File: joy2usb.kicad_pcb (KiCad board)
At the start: 2 copper layers, 55 x 90 mm, 18 parts, among them J1 DB9_Male, J2 Conn_02x04_Odd_Even, SW1 RST, SW2 SW_SPDT, U1 Arduino_Pro_Micro, U2 4066

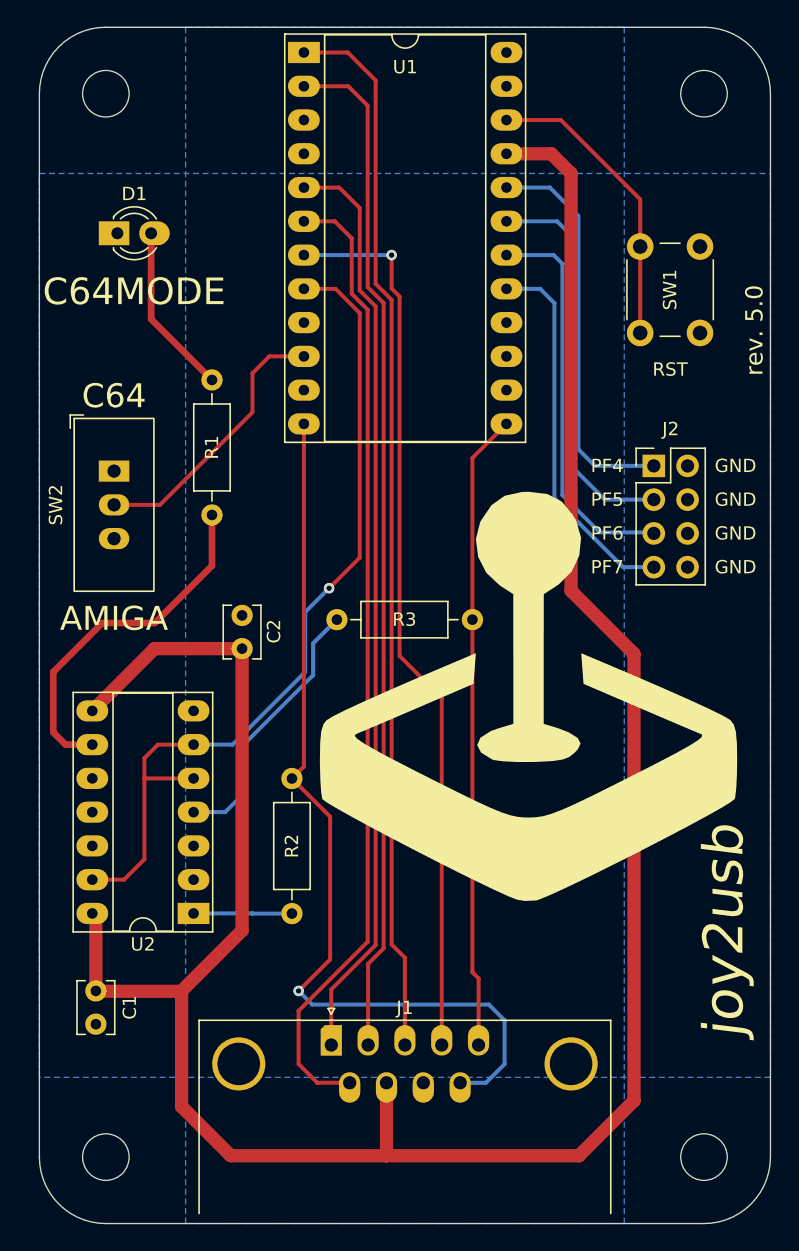
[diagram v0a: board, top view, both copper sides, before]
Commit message: PCB Rev. 6.2
removal of ic 4066
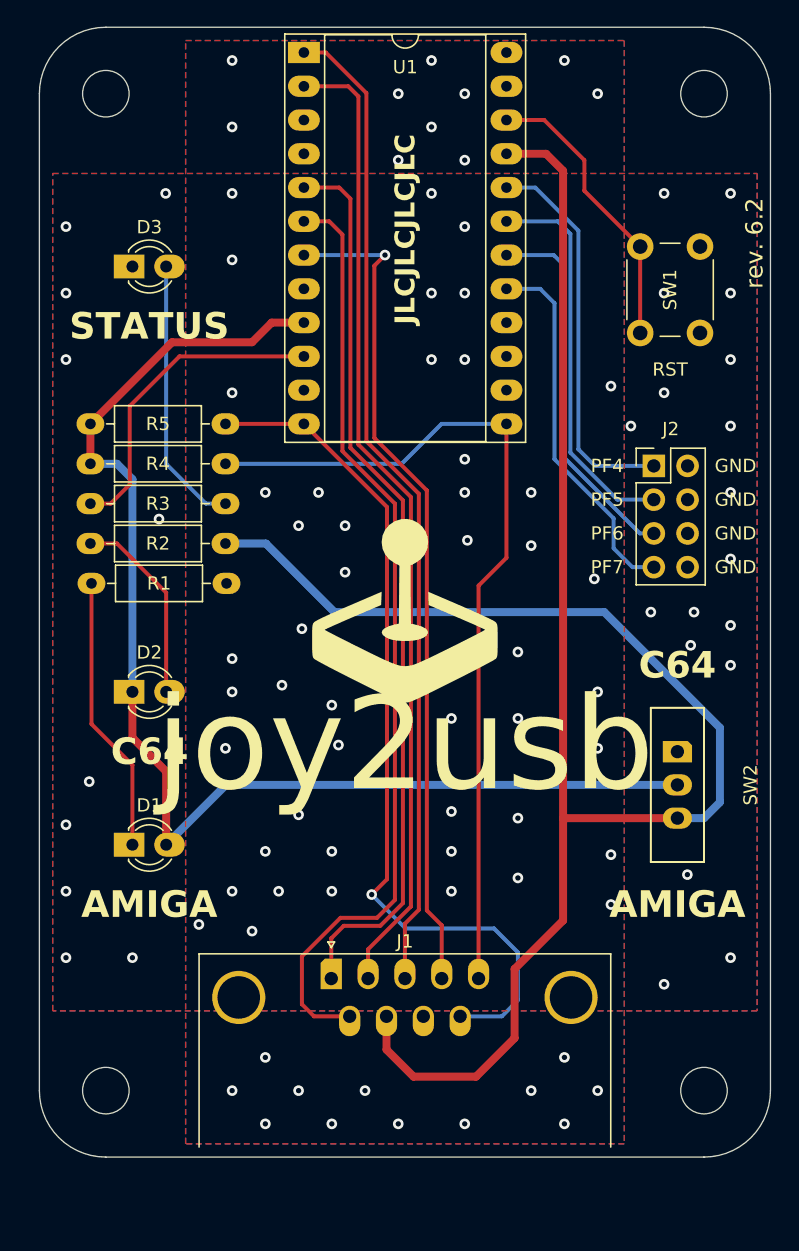
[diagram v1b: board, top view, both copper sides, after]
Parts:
- removed C1, C2: 100nF, Capacitor_THT:C_Disc_D3.8mm_W2.6mm_P2.50mm
- removed the G*** at (149.8, 105.5)
- removed REF**: OSHW-Logo_28.5x30mm_SilkScreen, Symbol:OSHW-Logo_28.5x30mm_SilkScreen
- removed U2: 4066, Package_DIP:DIP-14_W7.62mm_Socket_LongPads
- added D2: C64, misc:LED_D3.0mm_Oval, F.Cu at (120.0, 105.0)
- added D3: STATUS, misc:LED_D3.0mm_Oval, F.Cu at (120.0, 73.0)
- added G***: LOGO, misc:Joystick_LOGO_14x14mm, F.Cu at (140.5, 99.0)
- added R4: R10KΩ, misc:R_Axial_DIN0207_L6.3mm_D2.5mm_P10.16mm_Horizontal_Oval, F.Cu at (127.0, 87.8)
- added R5: RxΩ, misc:R_Axial_DIN0207_L6.3mm_D2.5mm_P10.16mm_Horizontal_Oval, F.Cu at (127.0, 84.8)
- D1: value C64MODE -> AMIGA; footprint Misc:LED_D3.0mm_Oval -> misc:LED_D3.0mm_Oval
- R1: value R220Ω -> RxΩ; footprint Resistor_THT:R_Axial_DIN0207_L6.3mm_D2.5mm_P10.16mm_Horizontal -> misc:R_Axial_DIN0207_L6.3mm_D2.5mm_P10.16mm_Horizontal_Oval
- R2: value R10KΩ -> RxΩ; footprint Resistor_THT:R_Axial_DIN0207_L6.3mm_D2.5mm_P10.16mm_Horizontal -> misc:R_Axial_DIN0207_L6.3mm_D2.5mm_P10.16mm_Horizontal_Oval
- R3: footprint Resistor_THT:R_Axial_DIN0207_L6.3mm_D2.5mm_P10.16mm_Horizontal -> misc:R_Axial_DIN0207_L6.3mm_D2.5mm_P10.16mm_Horizontal_Oval
- SW2: value SW_SPDT -> C64MODESW; footprint Misc:MFP_1220_KNITTER_SWITCH_SPDT_Oval -> misc:E-Switch-EG1218-Manufacturer_Recommended_Oval
- moved SW2 51.6 mm to (161.0, 109.5), turned to -90 degrees
- moved D1 46.0 mm to (120.0, 116.5)
- moved R3 20.5 mm to (127.0, 90.8)
- moved R2 18.4 mm to (127.0, 93.8), turned to 180 degrees
- moved R1 5.26 mm to (127.1, 96.8), turned to 180 degrees
- moved H1 5.00 mm to (118.0, 135.0)
- moved H4 5.00 mm to (163.0, 135.0)
- moved J1 5.00 mm to (135.0, 126.6)
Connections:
- D1 pad 1: GND -> Net-(D1-K)
- D1 pad 2: Net-(D1-Pad2) -> /F2F3MODE
- R1 pad 1: Net-(R1-Pad1) -> GND
- R1 pad 2: Net-(D1-Pad2) -> Net-(D1-K)
- R2 pad 1: /F2BTN -> VCC
- R3 pad 1: /F3BTN -> Net-(D3-A)
- R3 pad 2: Net-(U2-Pad4) -> Net-(U1-Digital7/PE6)
- SW2 pad 2: Net-(SW2-Pad2) -> /F2F3MODE
- SW2 pad 3: unconnected-(SW2-Pad3) -> VCC
- U1 pad 10: Net-(SW2-Pad2) -> Net-(U1-Digital7/PE6)
- U1 pad 8: /F2F3MODE -> unconnected-(U1-Digital5/PC6-Pad8)
- U1 pad 9: unconnected-(U1-Pad9) -> /F2F3MODE
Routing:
- net VCC: track 181.9 -> 146.6 mm
- net /F2F3MODE: track 64.3 -> 94.7 mm, vias 1 -> 0
- net Net-(R1-Pad1): track 26.9 -> 0.00 mm
- net Net-(U1-Digital7/PE6): track 0.00 -> 24.1 mm
- net Net-(D1-K): track 0.00 -> 20.9 mm
- net Net-(D3-A): track 0.00 -> 20.7 mm
- net Net-(SW2-Pad2): track 20.6 -> 0.00 mm
- net Net-(U2-Pad4): track 20.3 -> 0.00 mm
- net /F3BTN: track 47.9 -> 65.0 mm
- net Net-(D1-Pad2): track 12.9 -> 0.00 mm
- net Net-(D2-A): track 6.98 -> 14.7 mm
- net /LBTN: track 79.8 -> 74.7 mm
- net /RBTN: track 67.6 -> 63.0 mm
- net /DBTN: track 77.1 -> 73.8 mm
- net /F2BTN: track 68.8 -> 66.1 mm
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- added copper zone on F.Cu, net GND
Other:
- board size 55 x 90 mm -> 55 x 85 mm
- board text added: "JLCJLCJLCJLC"

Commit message: PCB Rev. 6.3
WayWayWay text on silkscreen for PCBWay is added
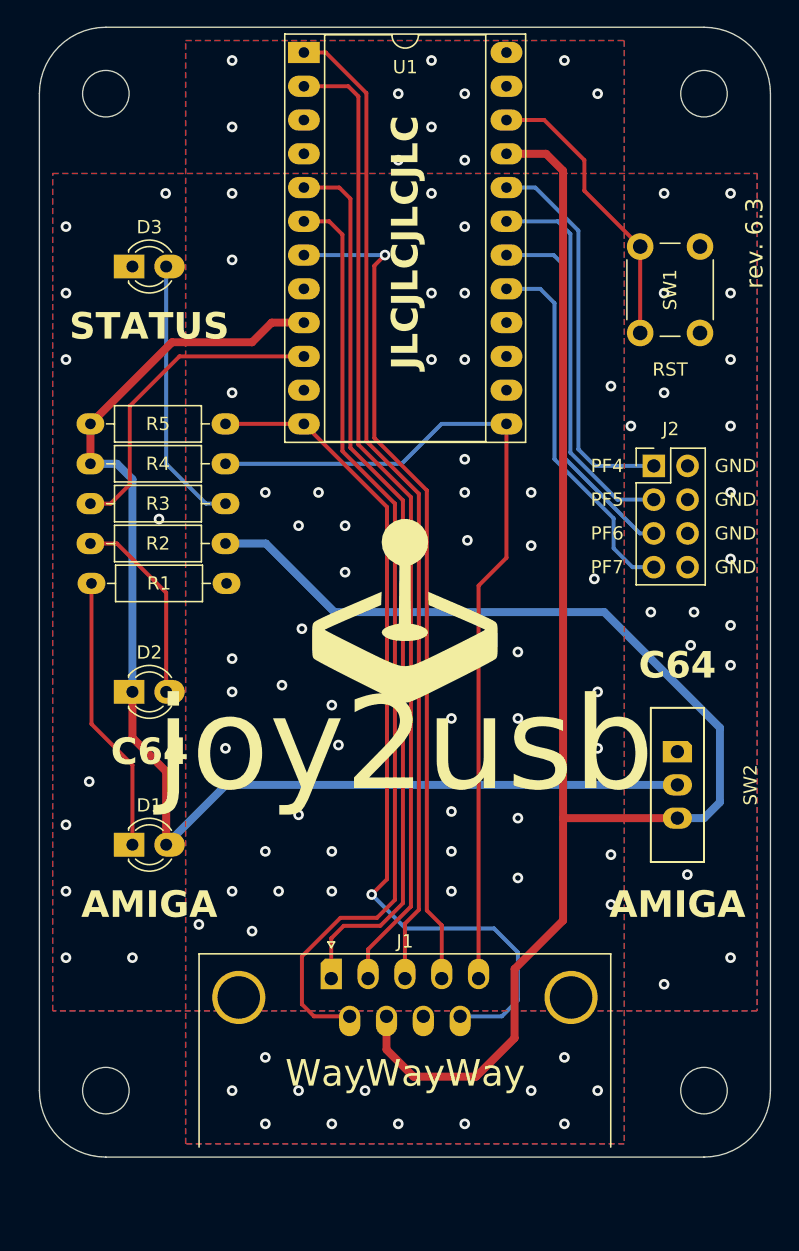
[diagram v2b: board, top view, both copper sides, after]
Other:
- board text added: "WayWayWay"
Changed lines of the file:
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@@
   (title_block
     (title "joy2usb")
-    (rev "6.2")
+    (rev "6.3")
     (company "mistepien@wp.pl")
   )
@@
     (effects (font (size 1.3 1.3) (thickness 0.3)))
   )
+  (gr_text "WayWayWay" (at 140.52 133.7) (layer "F.SilkS")
+    (effects (font (size 2 2) (thickness 0.3)))
+  )
   (gr_text "${TITLE}" (at 140.5 109) (layer "F.SilkS")
     (effects (font (face "C64") (size 7 7) (thickness 0.5)))
@@
     )
   )
-  (gr_text "JLCJLCJLCJLC" (at 140.52 70.2 90) (layer "F.SilkS")
-    (effects (font (size 1.5 1.5) (thickness 0.3) bold))
+  (gr_text "JLCJLCJLCJLC" (at 140.52 71.2 90) (layer "F.SilkS")
+    (effects (font (size 2 2) (thickness 0.3) bold))
   )
   (dimension (type aligned) (layer "Dwgs.User")
@@
   (segment (start 141.55 121.395584) (end 140.5 122.445584) (width 0.3) (layer "F.Cu") (net 3))
   (segment (start 142.15 121.444112) (end 143.27 122.564112) (width 0.3) (layer "F.Cu") (net 4))
+  (segment (start 142.15 89.84736) (end 142.15 121.444112) (width 0.3) (layer "F.Cu") (net 4))
+  (segment (start 143.27 122.564112) (end 143.27 126.569669) (width 0.3) (layer "F.Cu") (net 4))
+  (segment (start 138.2 72.94) (end 138.2 85.89736) (width 0.3) (layer "F.Cu") (net 4))
   (segment (start 139 72.14) (end 138.2 72.94) (width 0.3) (layer "F.Cu") (net 4))
   (segment (start 138.2 85.89736) (end 142.15 89.84736) (width 0.3) (layer "F.Cu") (net 4))
-  (segment (start 142.15 89.84736) (end 142.15 121.444112) (width 0.3) (layer "F.Cu") (net 4))
-  (segment (start 138.2 72.94) (end 138.2 85.89736) (width 0.3) (layer "F.Cu") (net 4))
-  (segment (start 143.27 122.564112) (end 143.27 126.569669) (width 0.3) (layer "F.Cu") (net 4))
   (via (at 139 72.14) (size 0.8) (drill 0.4) (layers "F.Cu" "B.Cu") (net 4))
   (segment (start 139 72.14) (end 132.9 72.14) (width 0.3) (layer "B.Cu") (net 4))

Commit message: added teardrops
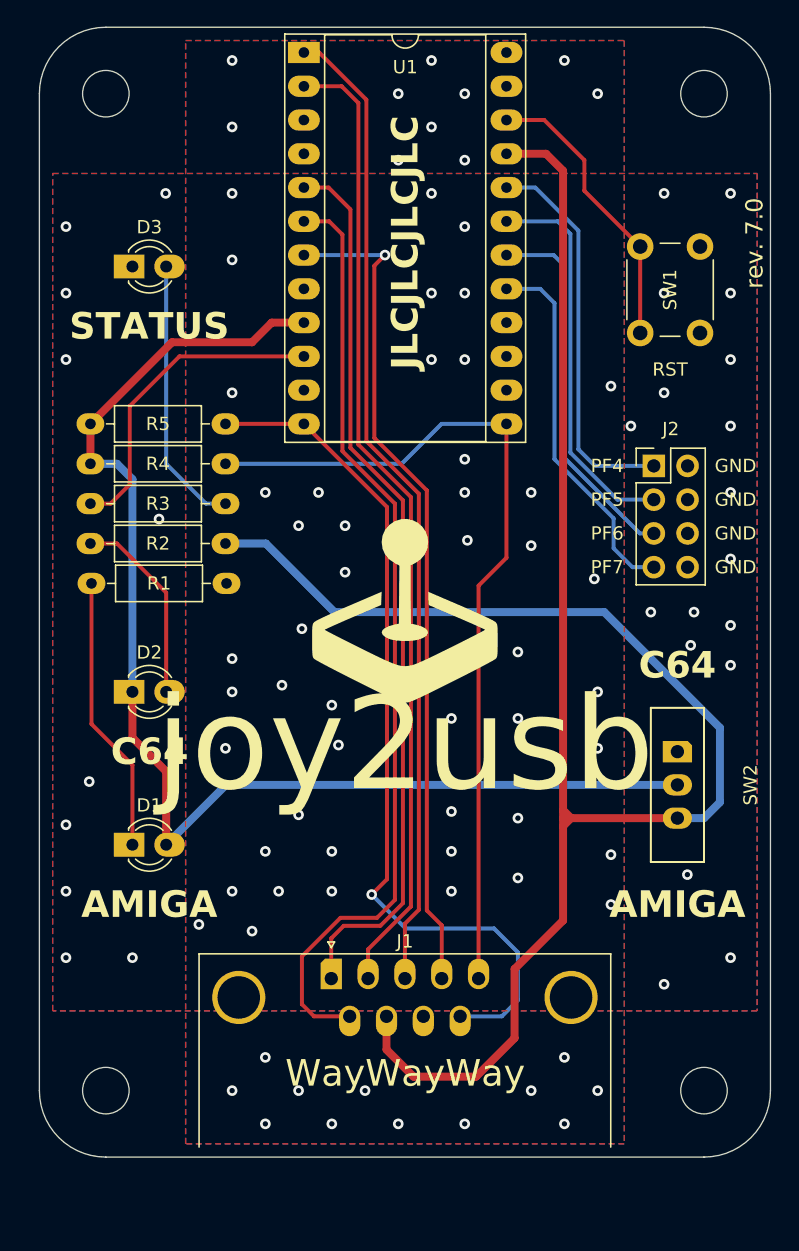
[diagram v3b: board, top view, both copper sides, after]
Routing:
- net VCC: track 146.6 -> 148.3 mm
